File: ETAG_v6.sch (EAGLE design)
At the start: 94 parts, among them CN2 PINHEAD-2x5-P1.27, IC2 SAMD21G18A-AUT, IC5 RTC_PCF8523T, IC6 EM4095, J1 22-27-2021-02, K1 G3VM-202J1, K2 G3VM-202J1, T1_VDIV P_CHANNEL_MOSFET_, U2 TC7SU04F, Y1 32.768kHz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

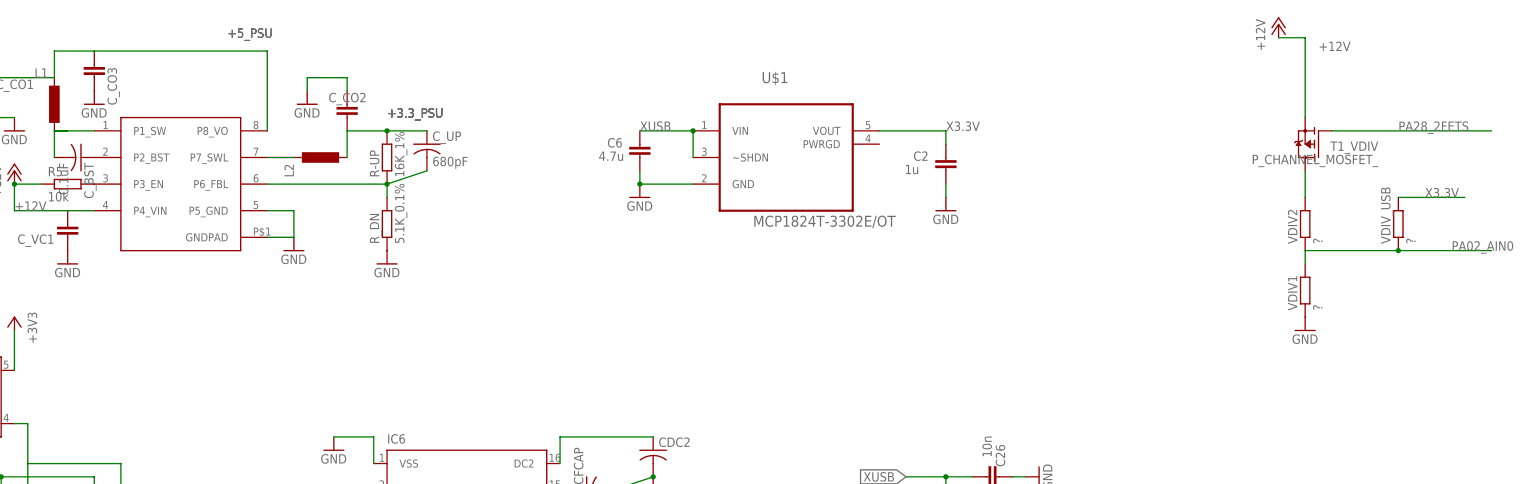
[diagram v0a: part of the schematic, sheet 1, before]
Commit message: dual level mosfet added to voltage divider
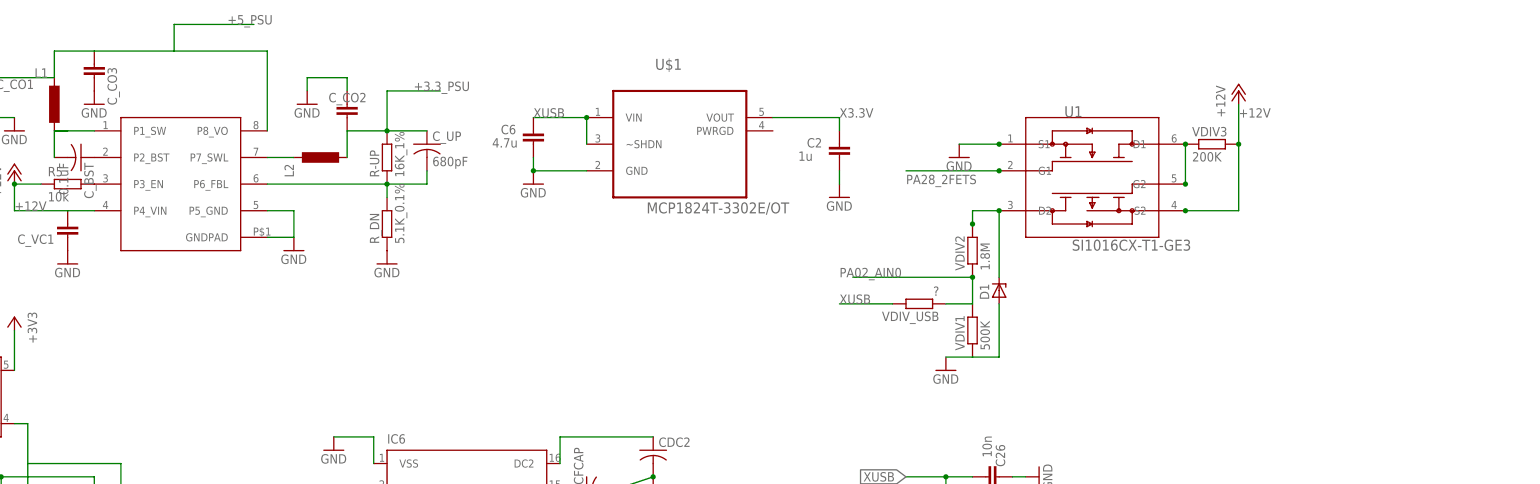
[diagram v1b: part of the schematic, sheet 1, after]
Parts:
- removed T1_VDIV: P_CHANNEL_MOSFET_, transistor-fet:P_CHANNEL_MOSFET_
- added D1: (no value), diode:ZENER-DIODESOD123
- added U1: SI1016CX-T1-GE3, Vishay_By_element14_Batch_1:SI1016CX-T1-GE3
- added VDIV3: 200K, Resistenze:2022_CR0603FW104L
- VDIV1: value ? -> 500K
- VDIV2: value ? -> 1.8M
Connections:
- removed net N$23: T1_VDIV.D, VDIV2.2
- new net N$15: U1.D1, U1.G2, VDIV3.1
- new net N$21: D1.C, U1.D2, VDIV2.2
- net +12V: now also U1.S2, VDIV3.2; no longer T1_VDIV.S
- net GND: now also D1.A, U1.S1
- net PA28_2FETS: now also U1.G1; no longer T1_VDIV.G
- net X3.3V: no longer VDIV_USB.2
- net XUSB: now also VDIV_USB.2
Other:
- moved on the sheet: C2, C6, U$1, VDIV1, VDIV2, VDIV_USB

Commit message: Design submitted to PCB shop
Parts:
- removed J1: 22-27-2021-02, con-molex:22-27-2021-02
- removed R3, R4: 0R, Resistenze:0233_0R_0603
- removed TP_10, TP_12, TP_A0, TP_A1, TP_A2, TP_A3, TP_A4, TP_AREF, TP_MOSI, TP_RESET, TP_SCK, TP_SCL, TP_SDA: TP_SP, SmartPrj:TP_SP
- added JP1: (no value), pinhead:PINHD-1X2
- added R10, R8: 10k, Resistenze:0028_CR0603JW103L
- added VAR_C: TZB4Z100AB10R00, mylibrary:TZB4Z100AB10R00
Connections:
- removed net PA10_MISO: TP_12.TESTP
- removed net SWCLK: CN2.4, R4.2
- removed net SWDIO: CN2.2, R3.1
- new net N$22: K1-1.K, K1-2.K, K2-1.K, K2-2.K, R8.2
- net GND: now also R10.1, R8.1; no longer K1-1.K, K1-2.K, K2-1.K, K2-2.K
- net N$11: now also VAR_C.P$2
- net N$12: now also VAR_C.P$1
- net PA02_AIN0: no longer TP_A0.TESTP
- net PA03_AREFA: no longer TP_AREF.TESTP
- net PA04_AIN4: no longer TP_A3.TESTP
- net PA05_AIN5: no longer TP_A4.TESTP
- net PA16_MOSI: no longer TP_MOSI.TESTP
- net PA17_SCK: no longer TP_SCK.TESTP
- net PA18_SS: no longer TP_10.TESTP
- net PA22_SDA: no longer TP_SDA.TESTP
- net PA23_SCL: no longer TP_SCL.TESTP
- net PA28_2FETS: now also R10.2
- net PA30_SWCLK: now also CN2.4; no longer R4.1
- net PA31_SWDIO: now also CN2.2; no longer R3.2
- net PB08_AIN2: no longer TP_A1.TESTP
- net PB09_AIN3: no longer TP_A2.TESTP
- net PB22_DEBUG_TX: now also JP1.2; no longer J1-2.S
- net PB23_DEBUG_RX: now also JP1.1; no longer J1-1.S
- net RESET: no longer TP_RESET.TESTP
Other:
- moved on the sheet: ANT1G$1, ANT1G$2, ANT2G$1, ANT2G$2, CDIV1, CDIV2, CRES, K1-1, K1-2, K2-1, K2-2, SJ1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
